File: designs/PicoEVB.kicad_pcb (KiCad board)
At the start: 6 copper layers, 34.3 x 8.4 mm, 129 parts, among them J1 Bus_PCI_Express_x4, J10 1P2, J11 1P0, J12 GND, J2 2.54mm Through-Hole Socket, J3 2.54mm Through-Hole Socket, J7 3P3, J8 1P8, J9 1P0, P2 USB_C_Plug_USB2.0, U1 XC7AxxT-xCSG325, U2 S25Q, U3 TPS82085SIL, U4 MAX1589AETT100T, U5 MIC47050-1.2YML, U6 TPS82085SIL, U7 FT230XQ

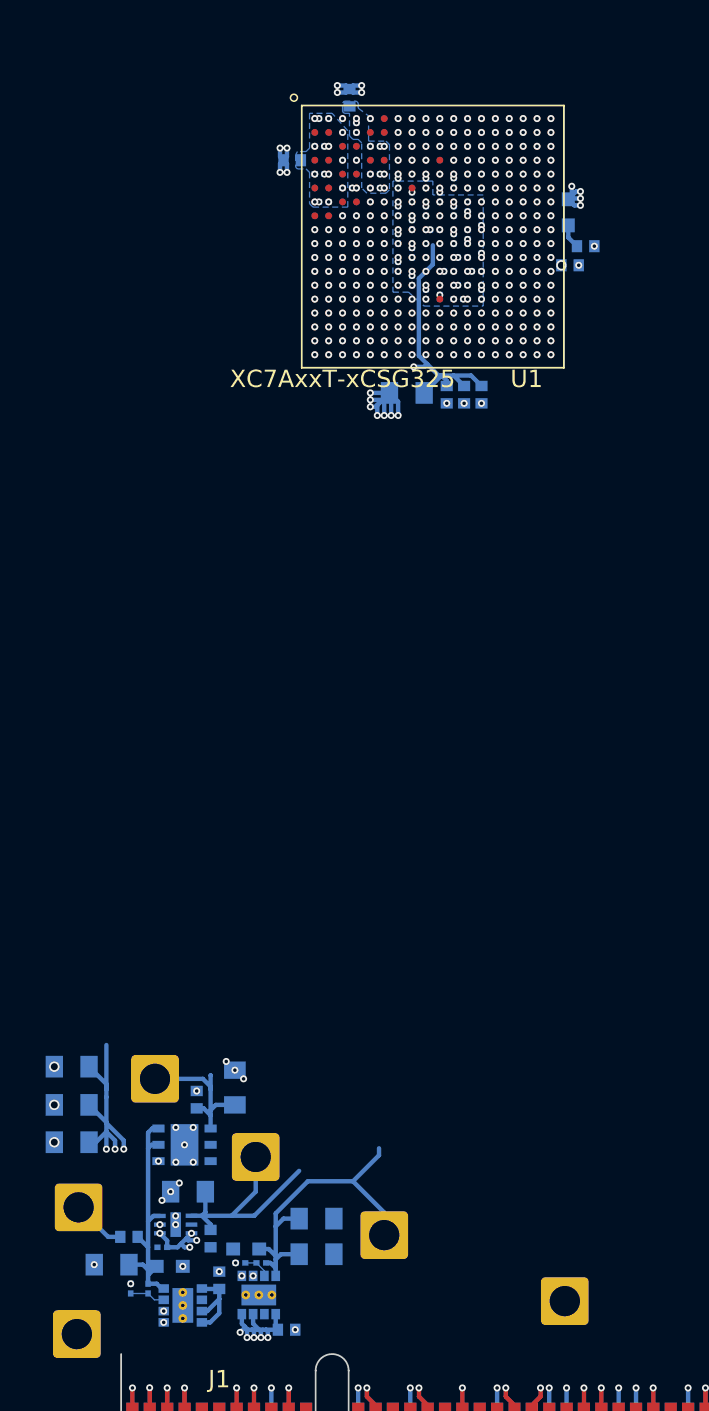
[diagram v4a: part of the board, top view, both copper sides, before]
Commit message: Completed Power Circuitry
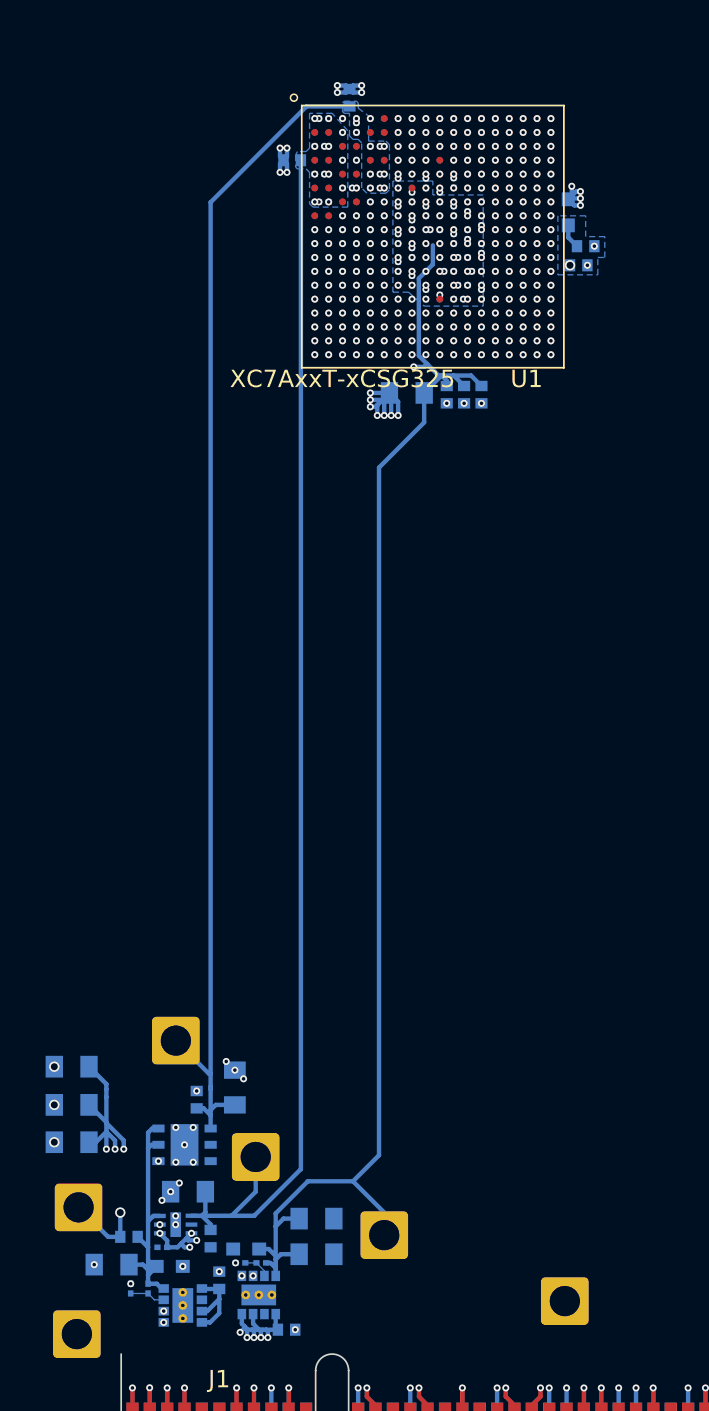
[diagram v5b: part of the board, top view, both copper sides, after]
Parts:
- moved J9 2.51 mm to (194.0, 105.5)
- moved C11 0.50 mm to (217.2, 60.9)
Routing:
- net P1V8_FPGA_VCCAUX_B: track 9.31 -> 77.8 mm, vias 7 -> 8
- net P1V0_MGTAVCC_B: track 9.09 -> 68.9 mm
- net P1V2_MGTAVTT_B: track 13.7 -> 72.0 mm
- net P1V0_VCC_FPGA_B: track 45.1 -> 89.7 mm
- net GND: track 96.6 -> 94.0 mm, vias 195 -> 196
- added copper zone on B.Cu, net P1V8_FPGA_VCCAUX_B

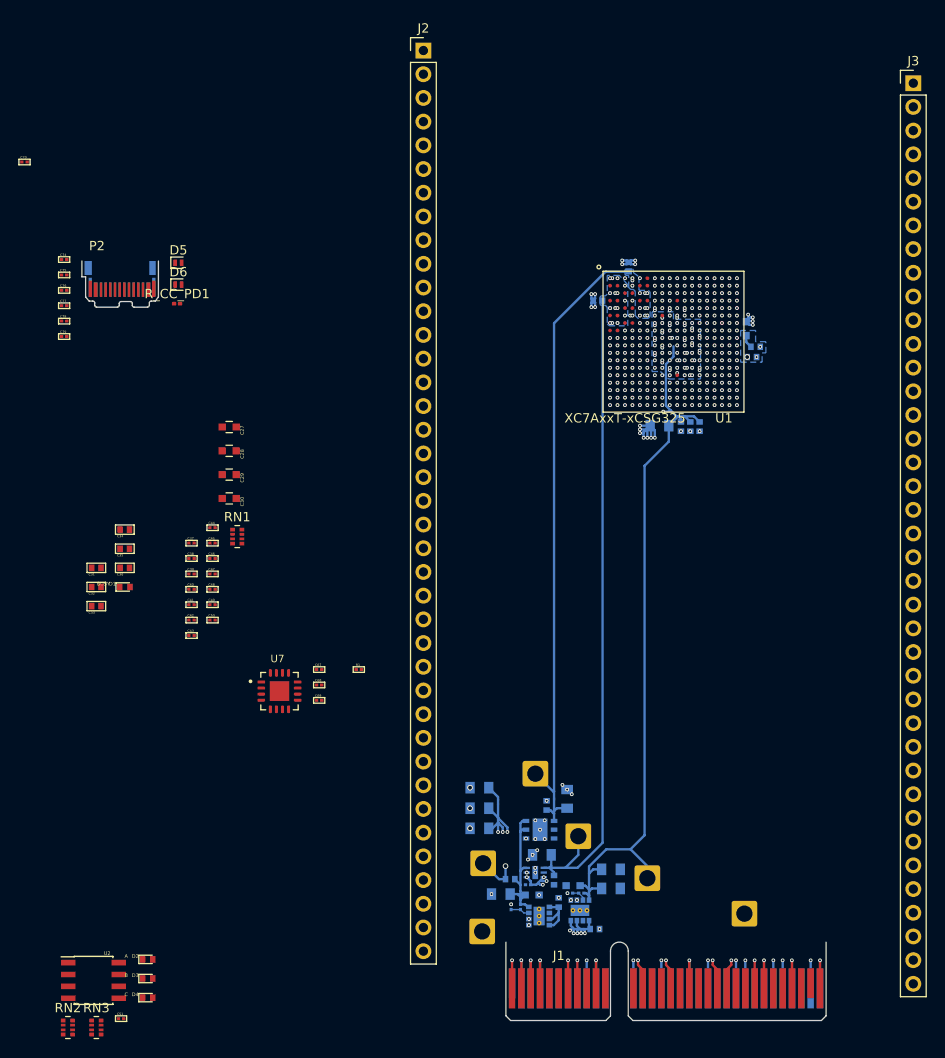
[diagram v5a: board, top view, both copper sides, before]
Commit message: progress 10% to USB JTAG
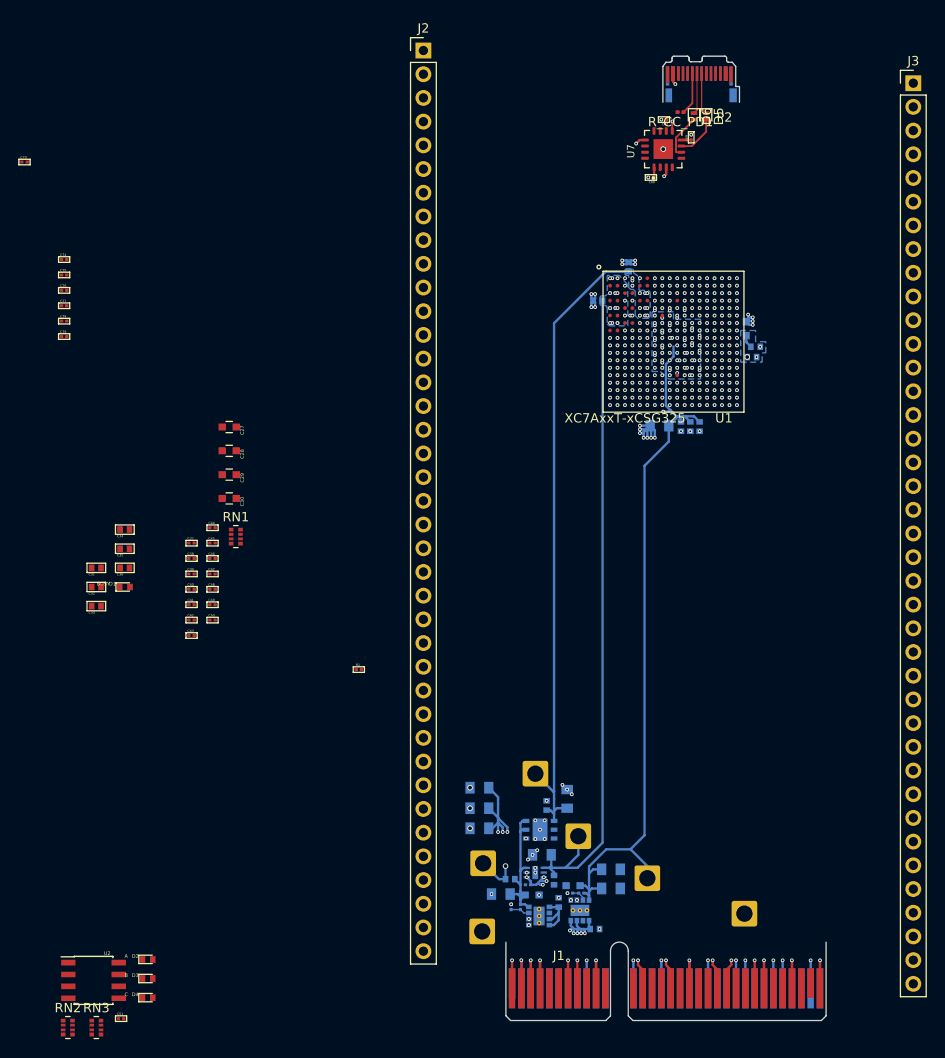
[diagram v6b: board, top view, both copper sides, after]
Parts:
- moved C69 72.3 mm to (210.7, 37.3), turned to 90 degrees
- moved U7 71.2 mm to (207.7, 38.6), turned to 90 degrees
- moved C67 69.6 mm to (207.8, 35.4), turned to 180 degrees
- moved P2 65.3 mm to (211.6, 31.6), turned to 180 degrees
- moved C68 65.0 mm to (206.4, 41.6), turned to 180 degrees
- moved D5 58.7 mm to (212.3, 35.0), turned to -90 degrees
- moved D6 58.1 mm to (211.0, 35.0), turned to -90 degrees
- moved R_CC_PD1 57.7 mm to (209.6, 34.6), turned to 180 degrees
- moved RN1 0.15 mm to (161.9, 80.1)
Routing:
- net Net-(U7-~{RESET}): track 0.00 -> 96.3 mm, vias 0 -> 1
- net USB_2+: track 0.00 -> 4.85 mm
- net USB_2-: track 0.00 -> 4.59 mm
- net Net-(P2-CC): track 0.00 -> 4.51 mm
- net Net-(D5-K): track 0.00 -> 4.42 mm
- net Net-(D6-K): track 0.00 -> 4.35 mm
- net GND: track 94.0 -> 97.4 mm, vias 196 -> 203
- net +3V3: track 43.0 -> 45.2 mm
